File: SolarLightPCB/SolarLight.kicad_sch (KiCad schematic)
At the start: 17 parts, among them J1 I2C, J2 SPI, U1 TP4056, U2 WeMos_D1_mini, U3 MCP1700-3302E

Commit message: PCB Improvements
- Remove the LED
- Make the pads biggger
- Add a GND Plane
- Add a logo
- Connect both GND and VCC pads of the mechanical neopixel pin
- Align positive / negative pins of Battery and solar panel
- Make GND Pads rectangular
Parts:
- removed D1: LED, LED_THT:LED_D5.0mm, symbol Device:LED
- removed R1: R, Resistor_THT:R_Axial_DIN0207_L6.3mm_D2.5mm_P2.54mm_Vertical, symbol Device:R
- JP2: footprint Resistor_THT:R_Box_L8.4mm_W2.5mm_P5.08mm -> Resistor_THT:R_Axial_DIN0204_L3.6mm_D1.6mm_P5.08mm_Horizontal
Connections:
- net +3V3: now also LIN1.1 (VCC)
- no-connect marks 5 -> 4
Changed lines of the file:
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@@
   )
   (no_connect (at 154.178 136.144))
-  (no_connect (at 154.178 133.604))
   (no_connect (at 136.144 76.2))
   (no_connect (at 128.524 93.98))
@@
     )
   )
-  (global_label "LED" (shape input) (at 112.268 91.948 90) (fields_autoplaced)
-    (effects (font (size 1.27 1.27)) (justify left))
-    (property "Intersheet References" "${INTERSHEET_REFS}" (id 0) (at 112.1886 86.0878 90)
-      (effects (font (size 1.27 1.27)) (justify left) hide)
-    )
-  )
   (global_label "MOSI" (shape input) (at 190.246 109.728 180) (fields_autoplaced)
     (effects (font (size 1.27 1.27)) (justify right))
@@
     (pin "2")
   )
-  (symbol (lib_id "Device:LED") (at 112.268 95.758 90) (unit 1)
-    (in_bom yes) (on_board yes) (fields_autoplaced)
-    (property "Reference" "D1" (id 0) (at 116.078 96.0754 90)
-      (effects (font (size 1.27 1.27)) (justify right))
-    )
-    (property "Value" "LED" (id 1) (at 116.078 98.6154 90)
-      (effects (font (size 1.27 1.27)) (justify right))
-    )
-    (property "Footprint" "LED_THT:LED_D5.0mm" (id 2) (at 112.268 95.758 0)
-      (effects (font (size 1.27 1.27)) hide)
-    )
-    (property "Datasheet" "~" (id 3) (at 112.268 95.758 0)
-      (effects (font (size 1.27 1.27)) hide)
-    )
-    (pin "1")
-    (pin "2")
-  )
   (symbol (lib_id "power:GND") (at 214.376 105.918 0) (unit 1)
     (in_bom yes) (on_board yes)
@@
     (pin "1")
   )
-  (symbol (lib_id "Device:R") (at 112.268 103.378 0) (unit 1)
-    (in_bom yes) (on_board yes) (fields_autoplaced)
-    (property "Reference" "R1" (id 0) (at 114.808 102.1079 0)
-      (effects (font (size 1.27 1.27)) (justify left))
-    )
-    (property "Value" "R" (id 1) (at 114.808 104.6479 0)
-      (effects (font (size 1.27 1.27)) (justify left))
-    )
-    (property "Footprint" "Resistor_THT:R_Axial_DIN0207_L6.3mm_D2.5mm_P2.54mm_Vertical" (id 2) (at 110.49 103.378 90)
-      (effects (font (size 1.27 1.27)) hide)
-    )
-    (property "Datasheet" "~" (id 3) (at 112.268 103.378 0)
-      (effects (font (size 1.27 1.27)) hide)
-    )
-    (pin "1")
-    (pin "2")
+  (symbol (lib_id "power:+3V3") (at 154.178 133.604 0) (unit 1)
+    (in_bom yes) (on_board yes)
+    (property "Reference" "#PWR?" (id 0) (at 154.178 137.414 0)
+      (effects (font (size 1.27 1.27)) hide)
+    )
+    (property "Value" "+3V3" (id 1) (at 153.289 129.921 0))
+    (property "Footprint" "" (id 2) (at 154.178 133.604 0)
+      (effects (font (size 1.27 1.27)) hide)
+    )
+    (property "Datasheet" "" (id 3) (at 154.178 133.604 0)
+      (effects (font (size 1.27 1.27)) hide)
+    )
+    (pin "1")
   )
   (symbol (lib_id "power:GND") (at 193.04 46.99 0) (unit 1)
@@
     )
     (property "Datasheet" "" (id 3) (at 193.04 46.99 0)
-      (effects (font (size 1.27 1.27)) hide)
-    )
-    (pin "1")
-  )
-  (symbol (lib_id "power:GND") (at 112.268 107.188 0) (unit 1)
-    (in_bom yes) (on_board yes) (fields_autoplaced)
-    (property "Reference" "#PWR0106" (id 0) (at 112.268 113.538 0)
-      (effects (font (size 1.27 1.27)) hide)
-    )
-    (property "Value" "GND" (id 1) (at 112.268 112.268 0))
-    (property "Footprint" "" (id 2) (at 112.268 107.188 0)
-      (effects (font (size 1.27 1.27)) hide)
-    )
-    (property "Datasheet" "" (id 3) (at 112.268 107.188 0)
       (effects (font (size 1.27 1.27)) hide)
     )
@@
       (effects (font (size 1.27 1.27)) hide)
     )
+    (pin "1")
+    (pin "2")
     (pin "3")
-    (pin "1")
-    (pin "2")
   )
   (symbol (lib_id "power:GND") (at 185.42 85.852 0) (unit 1)
@@
     (property "Reference" "JP2" (id 0) (at 183.007 103.505 0))
     (property "Value" "Bridge" (id 1) (at 181.737 105.156 0))
-    (property "Footprint" "Resistor_THT:R_Box_L8.4mm_W2.5mm_P5.08mm" (id 2) (at 185.166 107.188 0)
+    (property "Footprint" "Resistor_THT:R_Axial_DIN0204_L3.6mm_D1.6mm_P5.08mm_Horizontal" (id 2) (at 185.166 107.188 0)
       (effects (font (size 1.27 1.27)) hide)
     )
@@
       (reference "#PWR0105") (unit 1) (value "+3V3") (footprint "")
     )
-    (path "/5bb2513f-2840-4d02-b9db-1353ad2fe148"
-      (reference "#PWR0106") (unit 1) (value "GND") (footprint "")
-    )
     (path "/e78c0649-b4a3-4f91-ac29-c9de53c1e159"
       (reference "#PWR0107") (unit 1) (value "+3V3") (footprint "")
@@
       (reference "#PWR0117") (unit 1) (value "GND") (footprint "")
     )
+    (path "/2c65fd9b-6b86-4de9-88d8-fcb1dcaf593d"
+      (reference "#PWR?") (unit 1) (value "+3V3") (footprint "")
+    )
     (path "/1b639698-fdc2-412d-93eb-4fc53c894eea"
       (reference "BT1") (unit 1) (value "Battery_Cell") (footprint "Connector_PinHeader_2.54mm:PinHeader_1x02_P2.54mm_Vertical")
@@
       (reference "C1") (unit 1) (value "C_Polarized") (footprint "Capacitor_THT:CP_Radial_D5.0mm_P2.00mm")
     )
-    (path "/27d936a7-2f51-42cd-8be9-098b9487cf16"
-      (reference "D1") (unit 1) (value "LED") (footprint "LED_THT:LED_D5.0mm")
-    )
     (path "/b014f64b-63d7-4679-a15c-8f4cf024b19d"
       (reference "J1") (unit 1) (value "I2C") (footprint "Connector_PinHeader_2.54mm:PinHeader_1x04_P2.54mm_Vertical")
@@
     )
     (path "/a04ab534-b3ff-41d2-b40f-b10866f1afa8"
-      (reference "JP2") (unit 1) (value "Bridge") (footprint "Resistor_THT:R_Box_L8.4mm_W2.5mm_P5.08mm")
+      (reference "JP2") (unit 1) (value "Bridge") (footprint "Resistor_THT:R_Axial_DIN0204_L3.6mm_D1.6mm_P5.08mm_Horizontal")
     )
     (path "/a7c8a88d-781a-4fef-ada5-cbae7e10a79c"
@@
       (reference "LOUT1") (unit 1) (value "LEDs_Out") (footprint "NeopixelStrip:LED-Strip")
     )
-    (path "/3b6930db-edc5-4a46-ae32-cdfcfa0f14bd"
-      (reference "R1") (unit 1) (value "R") (footprint "Resistor_THT:R_Axial_DIN0207_L6.3mm_D2.5mm_P2.54mm_Vertical")
-    )
     (path "/d85e1e13-e38e-4950-90e0-28ee56a30aec"

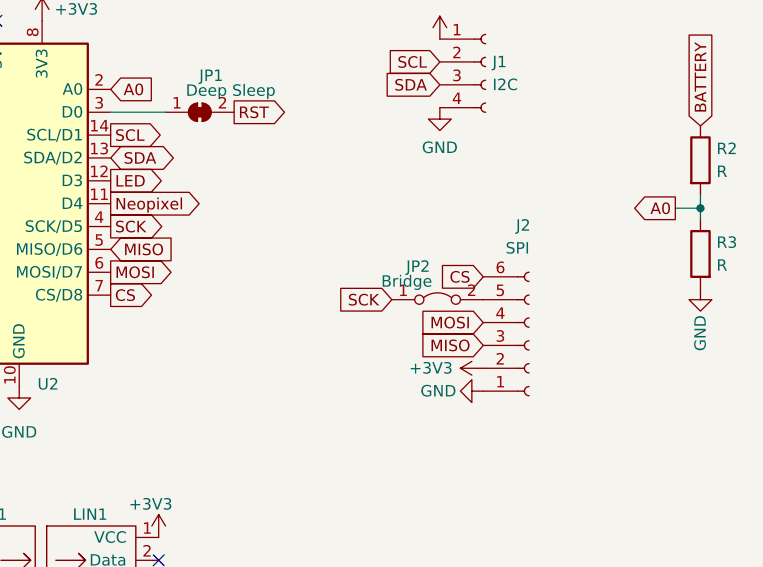
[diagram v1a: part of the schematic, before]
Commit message: Move the SPI header
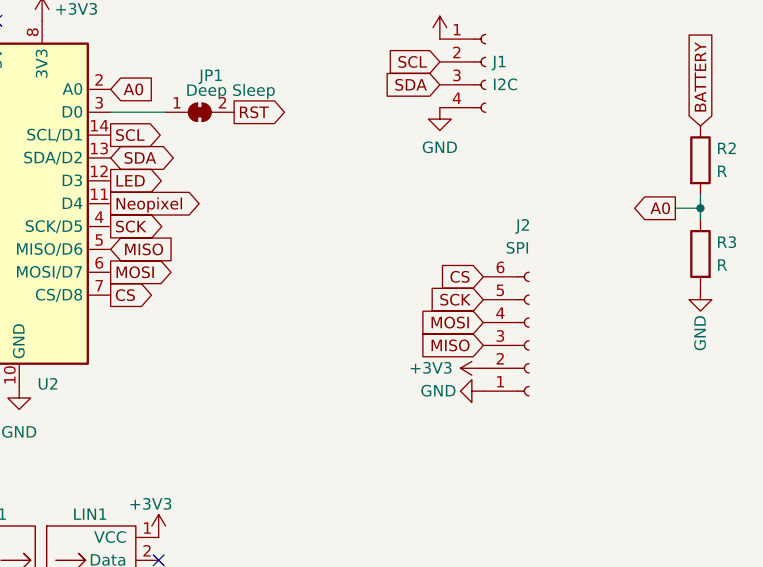
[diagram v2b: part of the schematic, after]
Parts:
- removed JP2: Bridge, Resistor_THT:R_Axial_DIN0204_L3.6mm_D1.6mm_P5.08mm_Horizontal, symbol Jumper:Jumper_2_Bridged
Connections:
- net SCK: now also J2.5 (Pin_5)
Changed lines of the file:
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@@
     )
   )
-  (global_label "SCK" (shape input) (at 180.086 107.188 180) (fields_autoplaced)
+  (global_label "SCK" (shape input) (at 190.246 107.188 180) (fields_autoplaced)
     (effects (font (size 1.27 1.27)) (justify right))
-    (property "Intersheet References" "${INTERSHEET_REFS}" (id 0) (at 173.9234 107.1086 0)
+    (property "Intersheet References" "${INTERSHEET_REFS}" (id 0) (at 184.0834 107.1086 0)
       (effects (font (size 1.27 1.27)) (justify right) hide)
     )
@@
   (symbol (lib_id "power:+3V3") (at 154.178 133.604 0) (unit 1)
     (in_bom yes) (on_board yes)
-    (property "Reference" "#PWR?" (id 0) (at 154.178 137.414 0)
+    (property "Reference" "#PWR0106" (id 0) (at 154.178 137.414 0)
       (effects (font (size 1.27 1.27)) hide)
     )
@@
     )
     (pin "1")
-  )
-  (symbol (lib_id "Jumper:Jumper_2_Bridged") (at 185.166 107.188 0) (unit 1)
-    (in_bom yes) (on_board yes)
-    (property "Reference" "JP2" (id 0) (at 183.007 103.505 0))
-    (property "Value" "Bridge" (id 1) (at 181.737 105.156 0))
-    (property "Footprint" "Resistor_THT:R_Axial_DIN0204_L3.6mm_D1.6mm_P5.08mm_Horizontal" (id 2) (at 185.166 107.188 0)
-      (effects (font (size 1.27 1.27)) hide)
-    )
-    (property "Datasheet" "~" (id 3) (at 185.166 107.188 0)
-      (effects (font (size 1.27 1.27)) hide)
-    )
-    (pin "1")
-    (pin "2")
   )
   (symbol (lib_id "Jumper:Jumper_2_Bridged") (at 169.545 38.608 0) (unit 1)
@@
       (reference "#PWR0105") (unit 1) (value "+3V3") (footprint "")
     )
+    (path "/2c65fd9b-6b86-4de9-88d8-fcb1dcaf593d"
+      (reference "#PWR0106") (unit 1) (value "+3V3") (footprint "")
+    )
     (path "/e78c0649-b4a3-4f91-ac29-c9de53c1e159"
       (reference "#PWR0107") (unit 1) (value "+3V3") (footprint "")
@@
       (reference "#PWR0117") (unit 1) (value "GND") (footprint "")
     )
-    (path "/2c65fd9b-6b86-4de9-88d8-fcb1dcaf593d"
-      (reference "#PWR?") (unit 1) (value "+3V3") (footprint "")
-    )
     (path "/1b639698-fdc2-412d-93eb-4fc53c894eea"
       (reference "BT1") (unit 1) (value "Battery_Cell") (footprint "Connector_PinHeader_2.54mm:PinHeader_1x02_P2.54mm_Vertical")
@@
       (reference "JP1") (unit 1) (value "Deep Sleep") (footprint "Jumper:SolderJumper-2_P1.3mm_Bridged_Pad1.0x1.5mm")
     )
-    (path "/a04ab534-b3ff-41d2-b40f-b10866f1afa8"
-      (reference "JP2") (unit 1) (value "Bridge") (footprint "Resistor_THT:R_Axial_DIN0204_L3.6mm_D1.6mm_P5.08mm_Horizontal")
-    )
     (path "/a7c8a88d-781a-4fef-ada5-cbae7e10a79c"

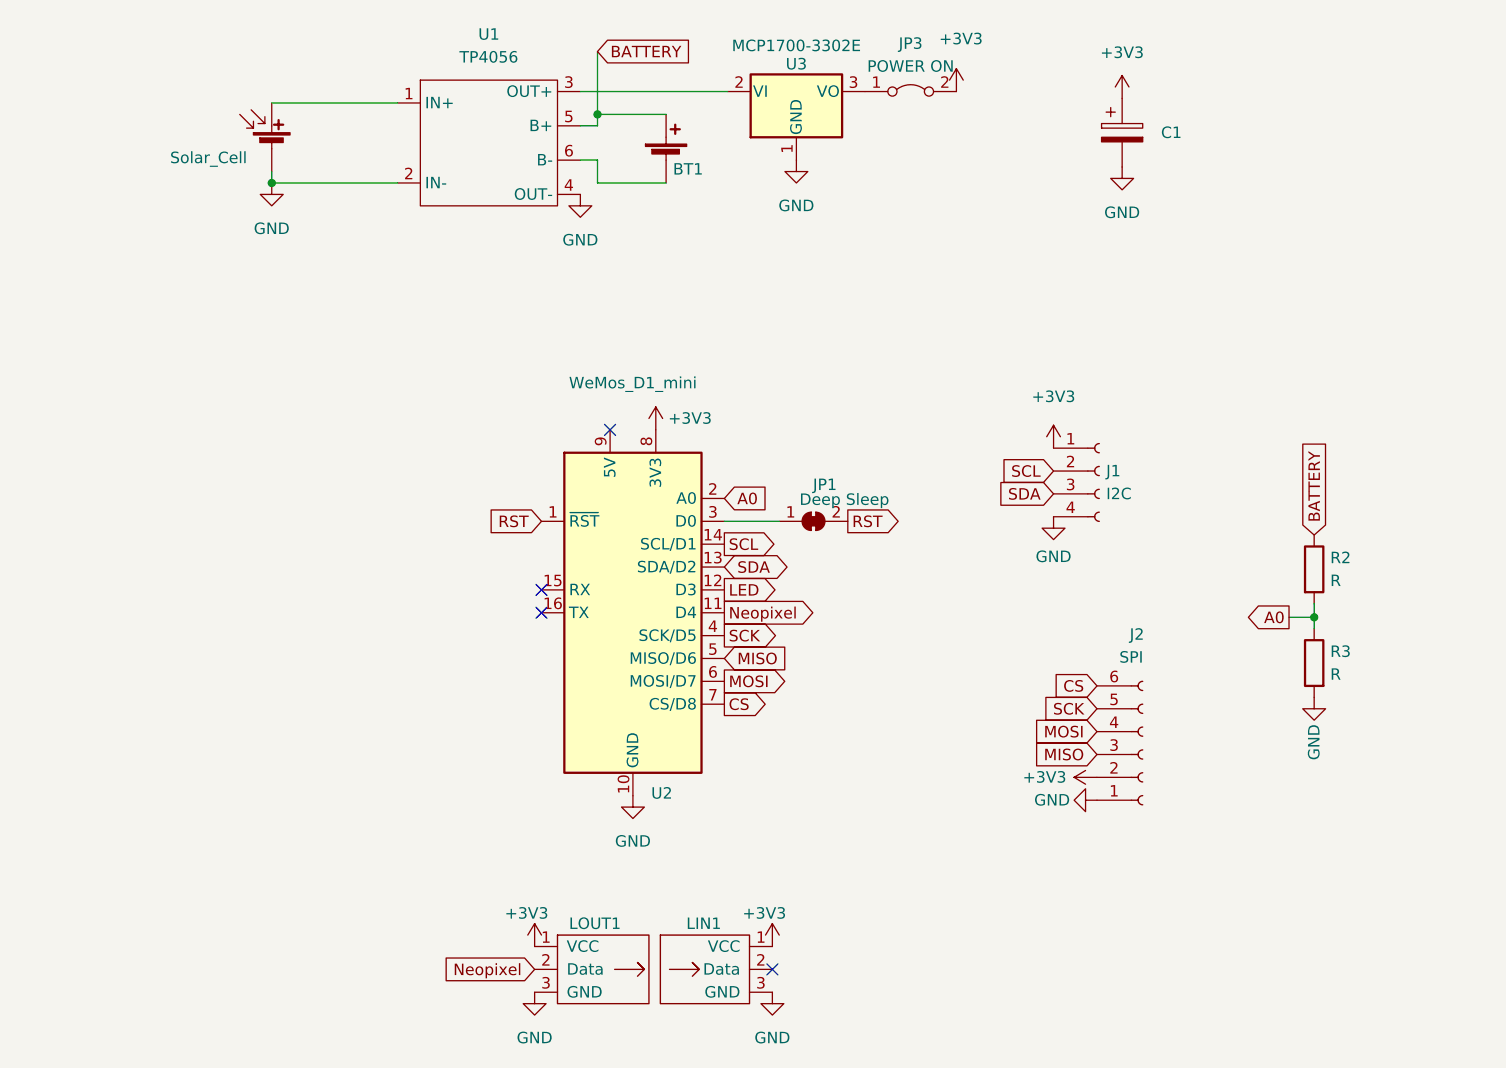
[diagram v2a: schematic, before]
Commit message: Add rotary encoder
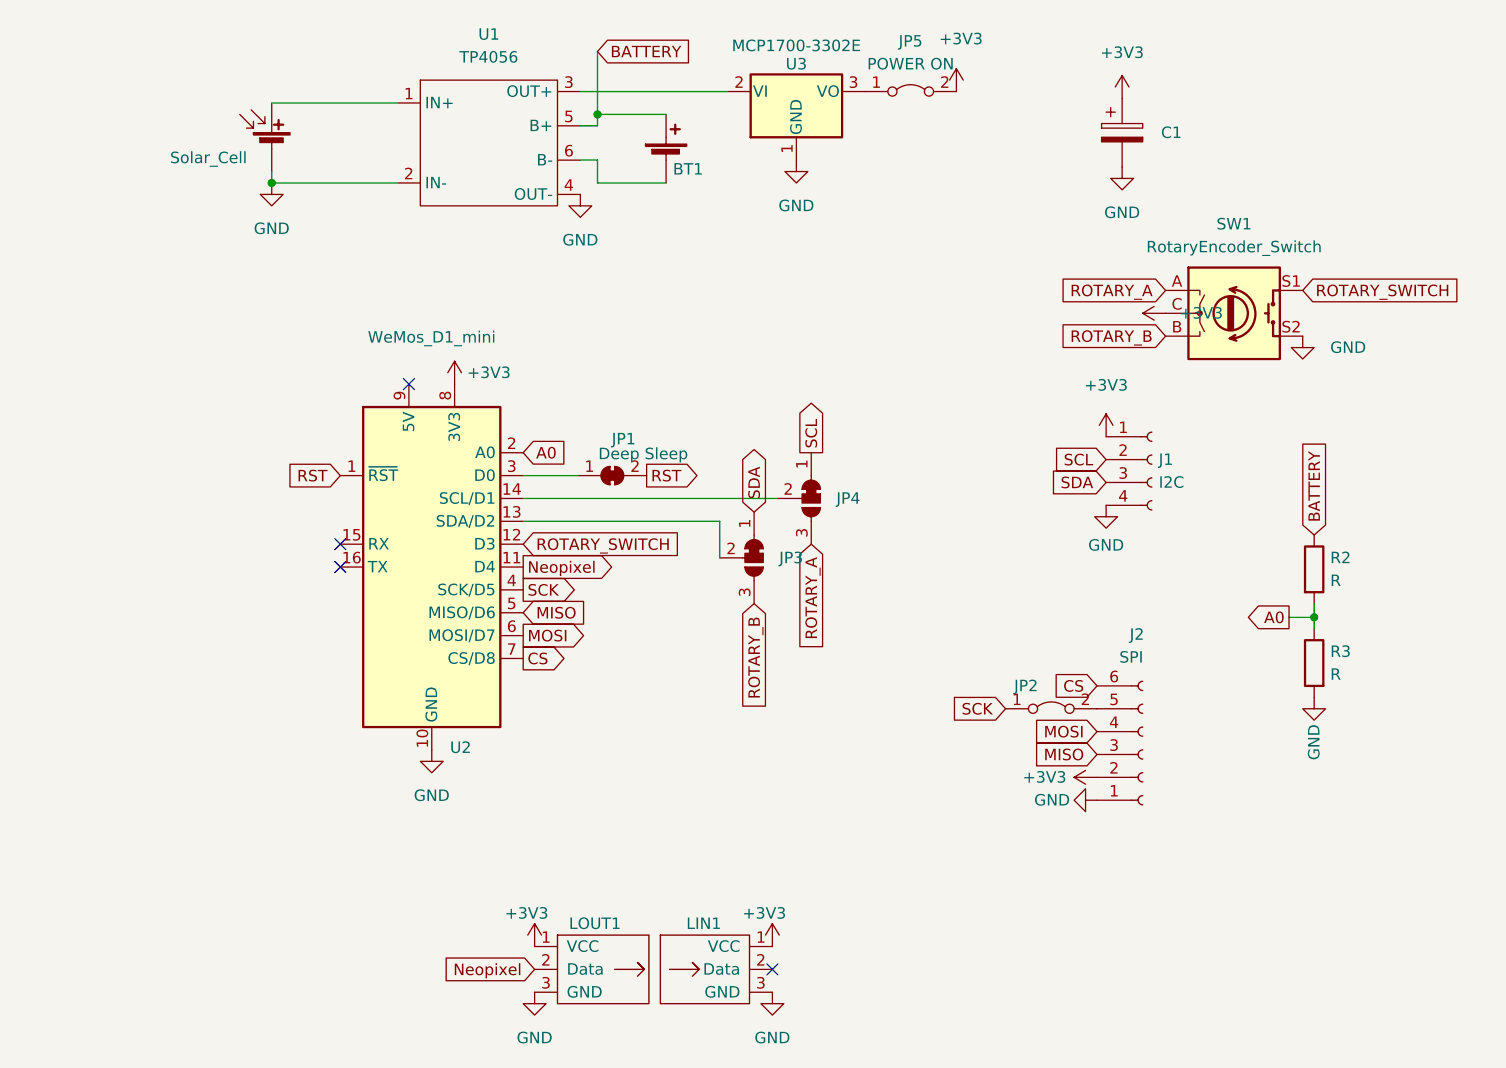
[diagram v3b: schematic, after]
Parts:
- added JP2: Jumper_2_Bridged, Resistor_THT:R_Axial_DIN0204_L3.6mm_D1.6mm_P5.08mm_Horizontal, symbol Jumper:Jumper_2_Bridged
- added JP3, JP4: SolderJumper_3_Bridged12, Jumper:SolderJumper-3_P1.3mm_Bridged12_Pad1.0x1.5mm, symbol Jumper:SolderJumper_3_Bridged12
- added SW1: RotaryEncoder_Switch, Rotary_Encoder:RotaryEncoder_Alps_EC12E-Switch_Vertical_H20mm, symbol Device:RotaryEncoder_Switch
- renumbered JP3 to JP5
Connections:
- net +3V3: now also SW1.C
- net GND: now also SW1.S2
- net SCK: now also JP2.1 (A); no longer J2.5 (Pin_5)
- net SCL: now also JP4.1 (A); no longer U2.14 (SCL/D1)
- net SDA: now also JP3.1 (A); no longer U2.13 (SDA/D2)
- net LED renamed ROTARY_SWITCH
- net ROTARY_SWITCH: now also SW1.S1
- new net: JP4.2 (C), U2.14 (SCL/D1)
- new net: J2.5 (Pin_5), JP2.2 (B)
- new net: JP3.2 (C), U2.13 (SDA/D2)
- new net ROTARY_A: JP4.3 (B), SW1.A
- new net ROTARY_B: JP3.3 (B), SW1.B
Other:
- moved on the sheet: J1, JP1, U2
